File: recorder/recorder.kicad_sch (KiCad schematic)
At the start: 14 parts, among them J1 GPIO_Conn_02x20_Odd_Even, U10 TPS7A4700RGWT, U2 ADAU7118

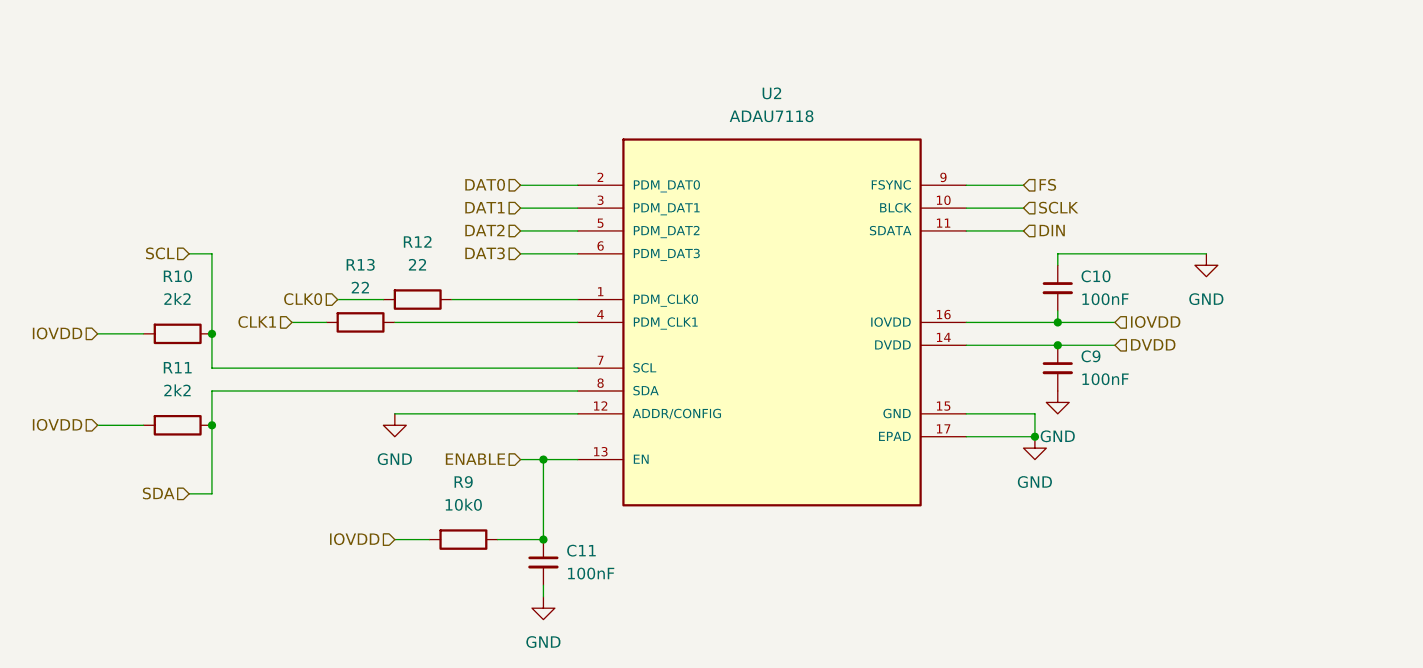
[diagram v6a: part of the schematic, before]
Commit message: removed pull up resistors for SDA/SCL, they are on the jetson board
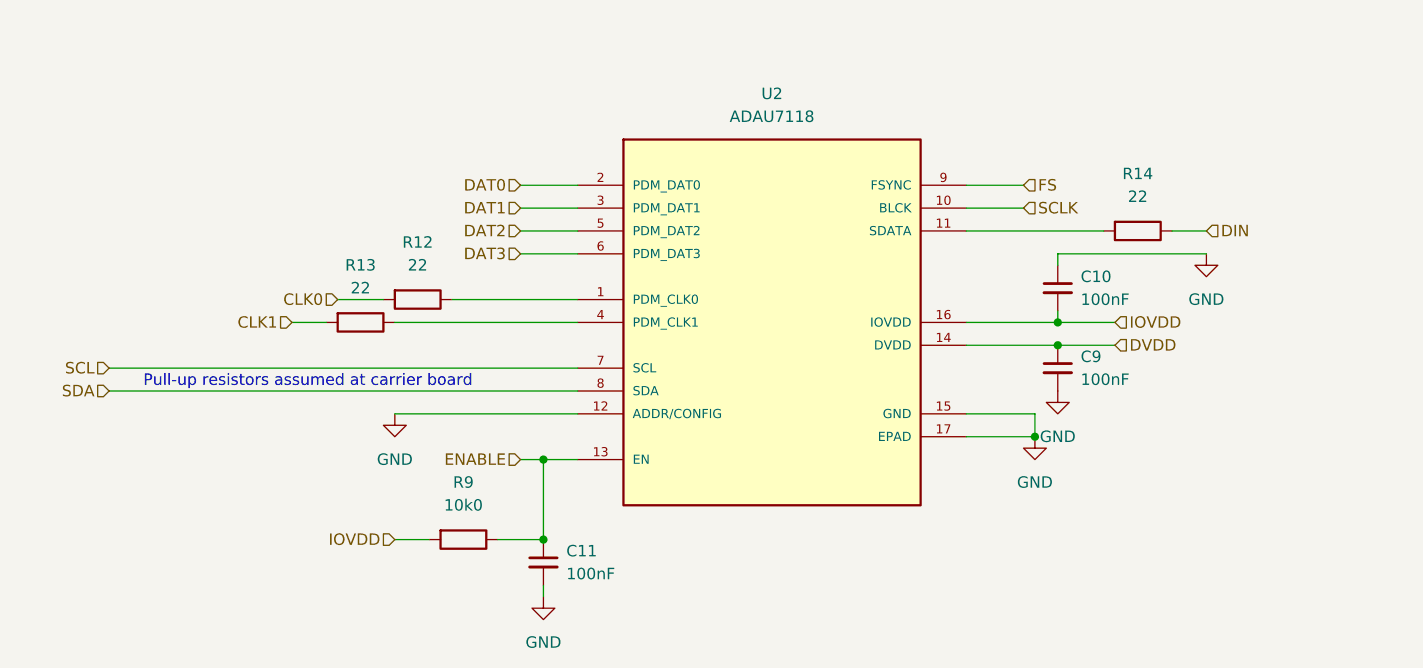
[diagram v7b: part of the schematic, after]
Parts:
- removed R10, R11: 2k2, Library:R_0603_1608Metric, symbol Device:R
- added R14: 22, Library:R_0603_1608Metric, symbol Device:R
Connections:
- net DIN: now also R14.1; no longer U2.11 (SDATA)
- new net: R14.2, U2.11 (SDATA)
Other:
- note added: "Pull-up resistors assumed at carrier board"

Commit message: MPN and Package
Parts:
- C10, C11, C12, C13, C14, C9: MPN (none) -> MCASJ168BD7475KTCA01; Package (none) -> 0603 (1608 Metric)
- J1: MPN (none) -> TSW-110-14-L-D; Manufacturer (none) -> Samtec; Package (none) -> 2x20 Pin Header, 2.54mm Pitch
- U10: MPN (none) -> TPS7A4700RGWT; Manufacturer (none) -> Texas Instruments; Package (none) -> VQFN-20
- U2: Availability Not in stock -> (none); Check_prices https://www.snapeda.com/parts/ADAU7118/Analog+Devices/view-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 -> (none); MF Analog Devices -> (none); MPN (none) -> ADAU7118ACPZRL; Manufacturer (none) -> Analog Devices; Package None -> LFCSP-16; Price None -> (none); SnapEDA_Link https://www.snapeda.com/parts/ADAU7118/Analog+Devices/view-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 -> (none)
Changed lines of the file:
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@@
+			)
+		)
+		(property "MPN" "MCASJ168BD7475KTCA01"
+			(at 77.47 104.14 0)
+			(effects
+				(font
+					(size 1.27 1.27)
+				)
+			)
+		)
+		(property "Package" "0603 (1608 Metric)"
+			(at 77.47 104.14 0)
+			(effects
+				(font
+					(size 1.27 1.27)
+				)
 			)
 		)
@@
 			)
 		)
+		(property "MPN" "TSW-110-14-L-D"
+			(at 214.63 82.55 0)
+			(effects
+				(font
+					(size 1.27 1.27)
+				)
+				(hide yes)
+			)
+		)
+		(property "Manufacturer" "Samtec"
+			(at 214.63 82.55 0)
+			(effects
+				(font
+					(size 1.27 1.27)
+				)
+				(hide yes)
+			)
+		)
+		(property "Package" "2x20 Pin Header, 2.54mm Pitch"
+			(at 214.63 82.55 0)
+			(effects
+				(font
+					(size 1.27 1.27)
+				)
+				(hide yes)
+			)
+		)
 		(pin "37"
 		)
@@
 			)
 		)
+		(property "MPN" "MCASJ168BD7475KTCA01"
+			(at 130.81 139.7 0)
+			(effects
+				(font
+					(size 1.27 1.27)
+				)
+			)
+		)
+		(property "Package" "0603 (1608 Metric)"
+			(at 130.81 139.7 0)
+			(effects
+				(font
+					(size 1.27 1.27)
+				)
+			)
+		)
 		(pin "1"
 		)
@@
 			)
 		)
+		(property "MPN" "MCASJ168BD7475KTCA01"
+			(at 134.62 73.66 0)
+			(effects
+				(font
+					(size 1.27 1.27)
+				)
+			)
+		)
+		(property "Package" "0603 (1608 Metric)"
+			(at 134.62 73.66 0)
+			(effects
+				(font
+					(size 1.27 1.27)
+				)
+			)
+		)
 		(pin "1"
 		)
@@
 			)
 		)
+		(property "MPN" "MCASJ168BD7475KTCA01"
+			(at 134.62 82.55 0)
+			(effects
+				(font
+					(size 1.27 1.27)
+				)
+			)
+		)
+		(property "Package" "0603 (1608 Metric)"
+			(at 134.62 82.55 0)
+			(effects
+				(font
+					(size 1.27 1.27)
+				)
+			)
+		)
 		(pin "2"
 		)
@@
 			)
 		)
+		(property "Package" "VQFN-20"
+			(at 82.55 137.16 0)
+			(effects
+				(font
+					(size 1.27 1.27)
+				)
+				(hide yes)
+			)
+		)
+		(property "MPN" "TPS7A4700RGWT"
+			(at 82.55 137.16 0)
+			(effects
+				(font
+					(size 1.27 1.27)
+				)
+				(hide yes)
+			)
+		)
+		(property "Manufacturer" "Texas Instruments"
+			(at 82.55 137.16 0)
+			(effects
+				(font
+					(size 1.27 1.27)
+				)
+				(hide yes)
+			)
+		)
 		(pin "13"
 		)
@@
 			)
 		)
+		(property "MPN" "MCASJ168BD7475KTCA01"
+			(at 73.66 139.7 0)
+			(effects
+				(font
+					(size 1.27 1.27)
+				)
+			)
+		)
+		(property "Package" "0603 (1608 Metric)"
+			(at 73.66 139.7 0)
+			(effects
+				(font
+					(size 1.27 1.27)
+				)
+			)
+		)
 		(pin "2"
 		)
@@
 			)
 		)
-		(property "MF" "Analog Devices"
+		(property "Manufacturer" "Analog Devices"
 			(at 104.14 74.93 0)
 			(effects
@@
 			)
 		)
-		(property "Package" "None"
-			(at 104.14 74.93 0)
-			(effects
-				(font
-					(size 1.27 1.27)
-				)
-				(justify bottom)
-				(hide yes)
-			)
-		)
-		(property "Price" "None"
-			(at 104.14 74.93 0)
-			(effects
-				(font
-					(size 1.27 1.27)
-				)
-				(justify bottom)
-				(hide yes)
-			)
-		)
-		(property "SnapEDA_Link" "https://www.snapeda.com/parts/ADAU7118/Analog+Devices/view-part/?ref=snap"
+		(property "Package" "LFCSP-16"
 			(at 104.14 74.93 0)
 			(effects
@@
 			)
 		)
-		(property "Availability" "Not in stock"
+		(property "MPN" "ADAU7118ACPZRL"
 			(at 104.14 74.93 0)
 			(effects
@@
 					(size 1.27 1.27)
 				)
-				(justify bottom)
-				(hide yes)
-			)
-		)
-		(property "Check_prices" "https://www.snapeda.com/parts/ADAU7118/Analog+Devices/view-part/?ref=eda"
-			(at 104.14 74.93 0)
-			(effects
-				(font
-					(size 1.27 1.27)
-				)
-				(justify bottom)
 				(hide yes)
 			)
@@
 			)
 		)
+		(property "MPN" "MCASJ168BD7475KTCA01"
+			(at 76.2 180.34 0)
+			(effects
+				(font
+					(size 1.27 1.27)
+				)
+			)
+		)
+		(property "Package" "0603 (1608 Metric)"
+			(at 76.2 180.34 0)
+			(effects
+				(font
+					(size 1.27 1.27)
+				)
+			)
+		)
